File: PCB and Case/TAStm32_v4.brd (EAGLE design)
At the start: 50 x 100 mm, 47 parts, among them IC1 74AVCH4T245PW,118, IC2 74AVCH4T245PW,118, IC3 74AVCH4T245PW,118, J1 ZX62D-B-5PA8, J10 RJSSE538002, J11 RJSSE538002, J12 SOICBITE, J13 CONSOLE_RESET, J2 UE27-AC54-100, J3 TSM-105-02-L-SHJ, J4 CONSOLE_RESET, J5 OLED128X64, J6 SAMTEC-TSM-116-01-X-SVJ, J7 SAMTEC-TSM-116-01-X-SVJ, U1 STM32F446RET6, U2 3.3V REG, Y1 8MHz

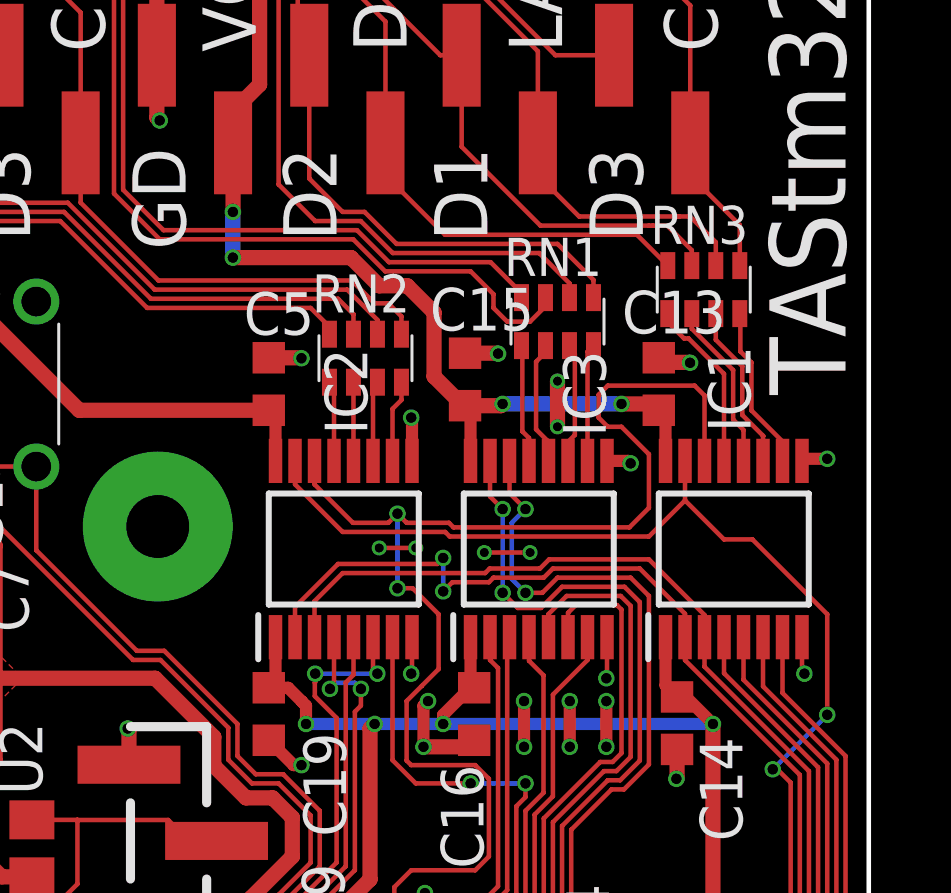
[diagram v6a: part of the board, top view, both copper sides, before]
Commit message: Pin reshuffle for proto
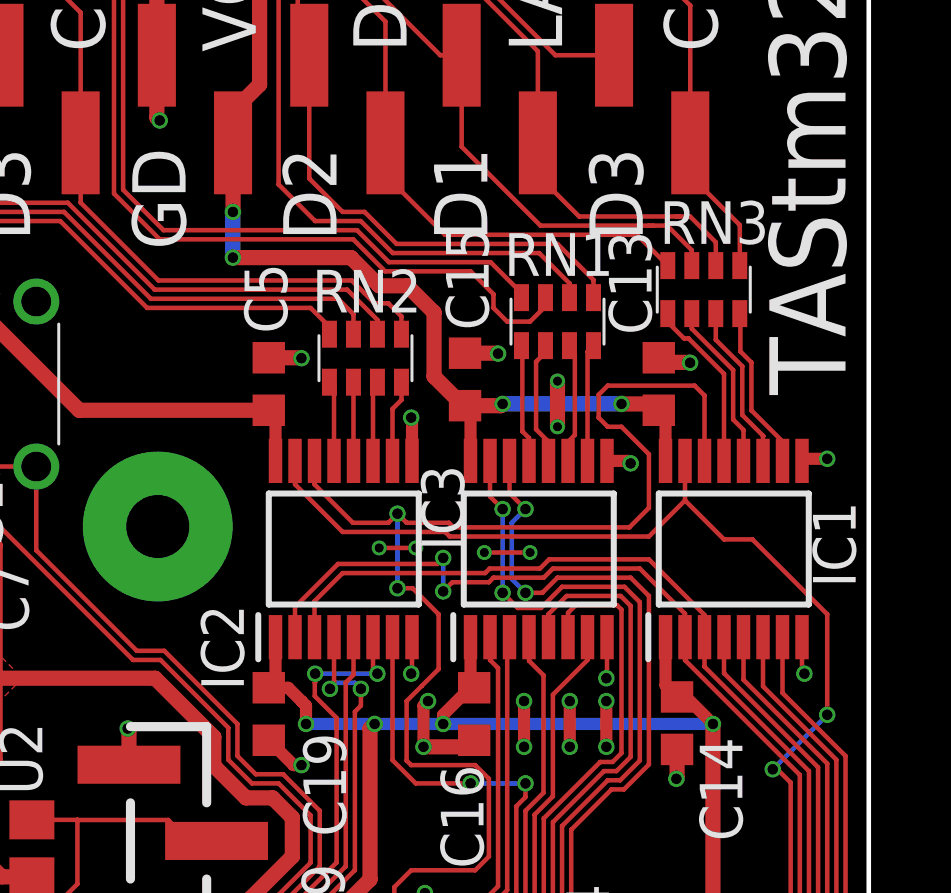
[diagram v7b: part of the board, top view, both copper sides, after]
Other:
- board text added: "design - rasteri / Ownasaurus"
- board text added: "github:Ownasaurus/TAStm32"
- board text removed: "design - rasteri / ownasaurus"
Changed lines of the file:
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@@
 <layer number="35" name="tGlue" color="7" fill="4" visible="no" active="yes"/>
 <layer number="36" name="bGlue" color="7" fill="5" visible="no" active="yes"/>
-<layer number="37" name="tTest" color="7" fill="1" visible="yes" active="yes"/>
+<layer number="37" name="tTest" color="7" fill="1" visible="no" active="yes"/>
 <layer number="38" name="bTest" color="7" fill="1" visible="no" active="yes"/>
 <layer number="39" name="tKeepout" color="4" fill="11" visible="no" active="yes"/>
@@
 <layer number="49" name="Reference" color="7" fill="1" visible="no" active="yes"/>
 <layer number="50" name="dxf" color="7" fill="1" visible="no" active="no"/>
-<layer number="51" name="tDocu" color="7" fill="1" visible="yes" active="yes"/>
+<layer number="51" name="tDocu" color="7" fill="1" visible="no" active="yes"/>
 <layer number="52" name="bDocu" color="7" fill="1" visible="no" active="yes"/>
 <layer number="53" name="tGND_GNDA" color="7" fill="9" visible="no" active="no"/>
@@
 <text x="43.2816" y="96.9264" size="1.9304" layer="25" font="vector" ratio="15" rot="R90">P1</text>
 <text x="8.5344" y="96.9264" size="1.9304" layer="25" font="vector" ratio="15" rot="R90">P2</text>
-<text x="47.1972" y="28.1084" size="1.9304" layer="26" font="vector" ratio="15" rot="MR90">design - rasteri / ownasaurus</text>
+<text x="54.5124" y="28.5656" size="1.9304" layer="26" font="vector" ratio="15" rot="MR90">design - rasteri / Ownasaurus</text>
 <text x="47.244" y="7.1628" size="1.9304" layer="25" font="vector" ratio="15" rot="R90">DFU</text>
 <polygon width="0.1524" layer="29">
@@
 <text x="29.5656" y="77.5716" size="1.778" layer="25" font="vector" ratio="15" rot="R90">VC</text>
 <text x="40.6908" y="74.3712" size="1.778" layer="25" font="vector" ratio="15" rot="R270">D3</text>
+<text x="57.408" y="28.5656" size="1.9304" layer="26" font="vector" ratio="15" rot="MR90">github:Ownasaurus/TAStm32</text>
 </plain>
 <attributes>
@@
 </element>
 <element name="C13" library="rcl" library_urn="urn:adsk.eagle:library:334" package="C0603K" package3d_urn="urn:adsk.eagle:package:23680/2" value="100nF" x="43" y="66.5" smashed="yes" rot="R270">
-<attribute name="NAME" x="41.7756" y="68.1864" size="1.4224" layer="25" font="vector" ratio="15"/>
+<attribute name="NAME" x="42.7608" y="68.1408" size="1.4224" layer="25" font="vector" ratio="15" rot="R90"/>
 <attribute name="POPULARITY" value="30" x="43" y="66.5" size="1.778" layer="27" rot="R270" display="off"/>
 <attribute name="SPICEPREFIX" value="C" x="43" y="66.5" size="1.778" layer="27" rot="R270" display="off"/>
@@
 <attribute name="MOUSER_PART_NUMBER" value="771-74AVCH4T245PW118" x="45.5" y="61" size="1.778" layer="27" rot="R90" display="off"/>
 <attribute name="MOUSER_PRICE-STOCK" value="http://www.mouser.com/Search/ProductDetail.aspx?qs=jquClx72t9DzXyE70aWLyQ%3d%3d" x="45.5" y="61" size="1.778" layer="27" rot="R90" display="off"/>
-<attribute name="NAME" x="45.3476" y="66.334" size="1.4224" layer="25" font="vector" ratio="15" rot="R90" align="center"/>
+<attribute name="NAME" x="48.8528" y="61.1524" size="1.4224" layer="25" font="vector" ratio="15" rot="R90" align="center"/>
 <attribute name="VALUE" x="45.5" y="61" size="1.27" layer="27" rot="R90" align="center"/>
 </element>
 <element name="C5" library="rcl" library_urn="urn:adsk.eagle:library:334" package="C0603K" package3d_urn="urn:adsk.eagle:package:23680/2" value="100nF" x="30" y="66.5" smashed="yes" rot="R270">
-<attribute name="NAME" x="29.1692" y="68.1404" size="1.4224" layer="25" font="vector" ratio="15"/>
+<attribute name="NAME" x="30.6148" y="68.1836" size="1.4224" layer="25" font="vector" ratio="15" rot="R90"/>
 <attribute name="POPULARITY" value="30" x="35.7912" y="66.5" size="1.778" layer="27" rot="R270" display="off"/>
 <attribute name="SPICEPREFIX" value="C" x="35.7912" y="66.5" size="1.778" layer="27" rot="R270" display="off"/>
@@
 <attribute name="MOUSER_PART_NUMBER" value="771-74AVCH4T245PW118" x="41.3392" y="55.5136" size="1.778" layer="27" rot="R90" display="off"/>
 <attribute name="MOUSER_PRICE-STOCK" value="http://www.mouser.com/Search/ProductDetail.aspx?qs=jquClx72t9DzXyE70aWLyQ%3d%3d" x="41.3392" y="55.5136" size="1.778" layer="27" rot="R90" display="off"/>
-<attribute name="NAME" x="32.5748" y="66.254" size="1.4224" layer="25" font="vector" ratio="15" rot="R270" align="center"/>
+<attribute name="NAME" x="28.46" y="57.7196" size="1.4224" layer="25" font="vector" ratio="15" rot="R270" align="center"/>
 <attribute name="VALUE" x="32.5" y="61" size="1.27" layer="27" rot="R90" align="center"/>
 </element>
 <element name="C15" library="rcl" library_urn="urn:adsk.eagle:library:334" package="C0603K" package3d_urn="urn:adsk.eagle:package:23680/2" value="100nF" x="36.5428" y="66.6524" smashed="yes" rot="R270">
-<attribute name="NAME" x="35.3748" y="68.2824" size="1.4224" layer="25" font="vector" ratio="15"/>
+<attribute name="NAME" x="37.3308" y="68.2932" size="1.4224" layer="25" font="vector" ratio="15" rot="R90"/>
 <attribute name="POPULARITY" value="30" x="42.334" y="66.6524" size="1.778" layer="27" rot="R270" display="off"/>
 <attribute name="SPICEPREFIX" value="C" x="42.334" y="66.6524" size="1.778" layer="27" rot="R270" display="off"/>
@@
 <attribute name="MOUSER_PART_NUMBER" value="771-74AVCH4T245PW118" x="47.8392" y="55.5136" size="1.778" layer="27" rot="R90" display="off"/>
 <attribute name="MOUSER_PRICE-STOCK" value="http://www.mouser.com/Search/ProductDetail.aspx?qs=jquClx72t9DzXyE70aWLyQ%3d%3d" x="47.8392" y="55.5136" size="1.778" layer="27" rot="R90" display="off"/>
-<attribute name="NAME" x="40.524" y="66.1816" size="1.4224" layer="25" font="vector" ratio="15" rot="R90" align="center"/>
+<attribute name="NAME" x="35.7996" y="62.3716" size="1.4224" layer="25" font="vector" ratio="15" rot="R90" align="center"/>
 <attribute name="VALUE" x="39" y="61" size="1.27" layer="27" rot="R90" align="center"/>
 </element>
@@
 <attribute name="MF" value="" x="39.624" y="68.58" size="1.778" layer="27" display="off"/>
 <attribute name="MPN" value="" x="39.624" y="68.58" size="1.778" layer="27" display="off"/>
-<attribute name="NAME" x="37.846" y="70.104" size="1.27" layer="25"/>
+<attribute name="NAME" x="37.846" y="70.104" size="1.4224" layer="25" font="vector" ratio="15"/>
 <attribute name="OC_FARNELL" value="unknown" x="39.624" y="68.58" size="1.778" layer="27" display="off"/>
 <attribute name="OC_NEWARK" value="unknown" x="39.624" y="68.58" size="1.778" layer="27" display="off"/>
@@
 <attribute name="MF" value="" x="33.2232" y="67.3608" size="1.778" layer="27" display="off"/>
 <attribute name="MPN" value="" x="33.2232" y="67.3608" size="1.778" layer="27" display="off"/>
-<attribute name="NAME" x="31.4452" y="68.8848" size="1.27" layer="25"/>
+<attribute name="NAME" x="31.4452" y="68.8848" size="1.4224" layer="25" font="vector" ratio="15"/>
 <attribute name="OC_FARNELL" value="unknown" x="33.2232" y="67.3608" size="1.778" layer="27" display="off"/>
 <attribute name="OC_NEWARK" value="unknown" x="33.2232" y="67.3608" size="1.778" layer="27" display="off"/>
@@
 <attribute name="MF" value="" x="44.5008" y="69.6468" size="1.778" layer="27" display="off"/>
 <attribute name="MPN" value="" x="44.5008" y="69.6468" size="1.778" layer="27" display="off"/>
-<attribute name="NAME" x="42.7228" y="71.1708" size="1.27" layer="25"/>
+<attribute name="NAME" x="43.0276" y="71.1708" size="1.4224" layer="25" font="vector" ratio="15"/>
 <attribute name="OC_FARNELL" value="unknown" x="44.5008" y="69.6468" size="1.778" layer="27" display="off"/>
 <attribute name="OC_NEWARK" value="unknown" x="44.5008" y="69.6468" size="1.778" layer="27" display="off"/>
@@
 <vertex x="20.8788" y="55.7784"/>
 </polygon>
+<wire x1="37.2618" y1="37.8234" x2="34.7952" y2="35.2044" width="0" layer="19" extent="1-1"/>
 </signal>
 <signal name="I2C_SCL">

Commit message: notes
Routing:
- net V+: track 267.6 -> 264.8 mm
- net P2_CLOCK: track 23.2 -> 22.6 mm
